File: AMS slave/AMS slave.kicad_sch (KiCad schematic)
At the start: 64 parts, among them J2 Conn_02x03_Odd_Even, J3 Conn_01x05, J4 Conn_01x05, Q2 AO3402, Q3 NCE60P04Y, SW2 SW_Push, U2 ATmega328P-A, U3 MCP2515-xST, U4 ISO1050DUB, U5 B0505MT-1WR4, U6 TPS54302, Y1 20MHz, Y2 8MHz

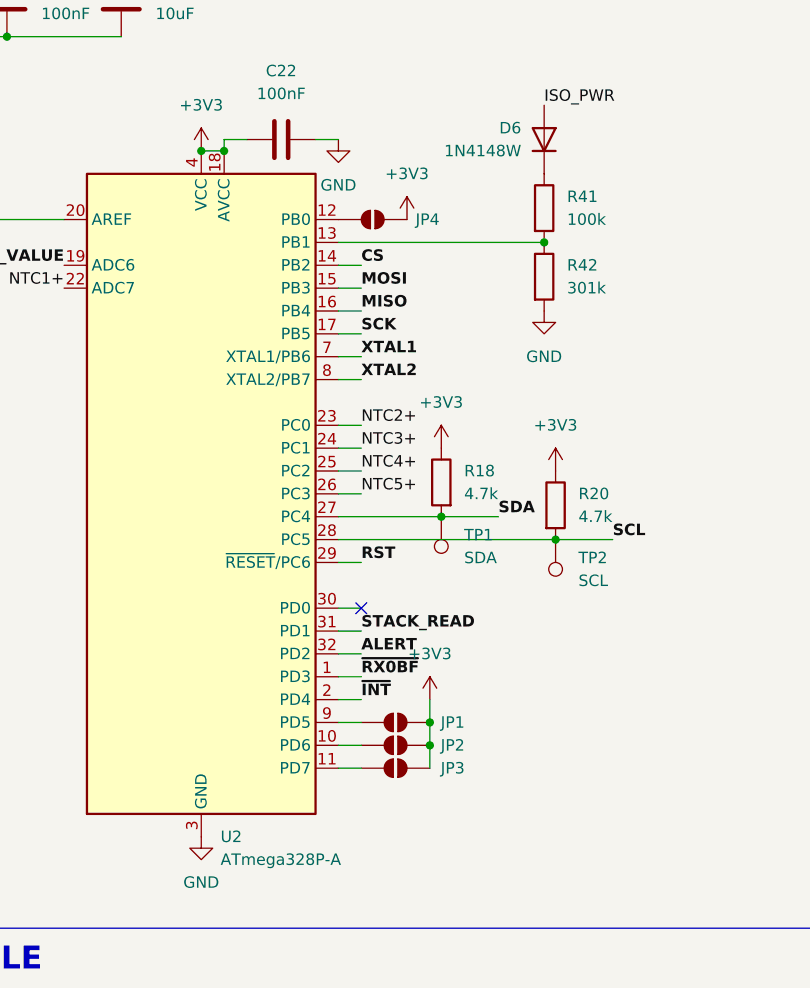
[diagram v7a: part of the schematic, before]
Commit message: Made slave select pads pull down
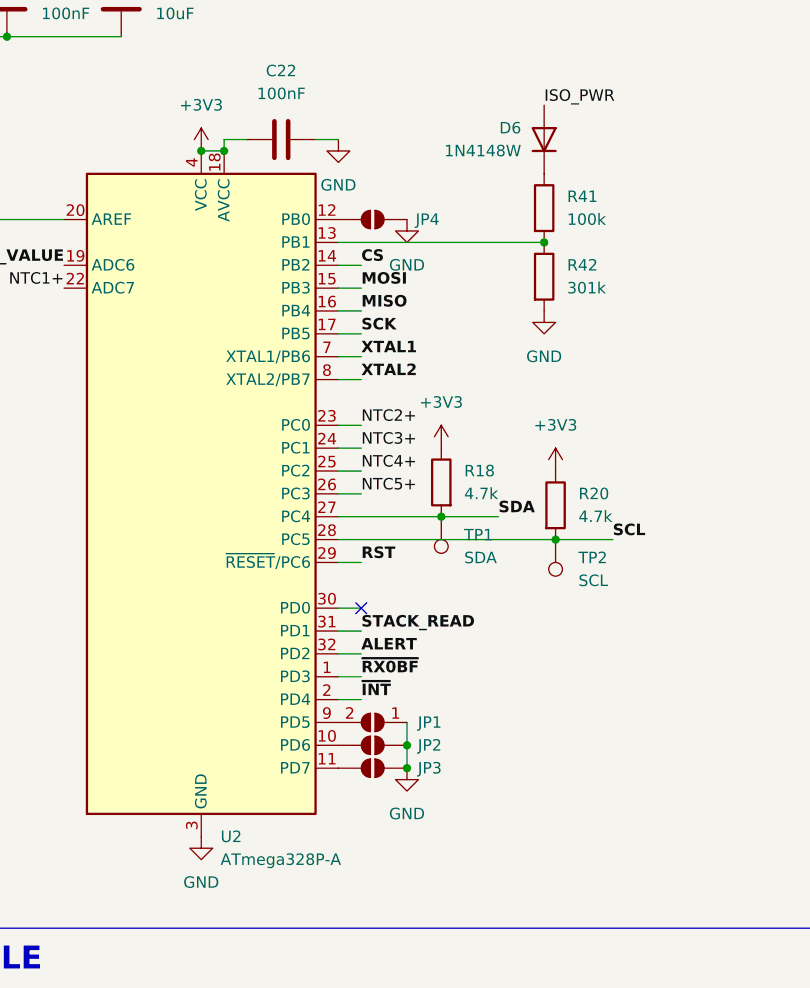
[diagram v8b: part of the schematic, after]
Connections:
- net +3V3: no longer JP1.2 (B), JP2.2 (B), JP3.2 (B), JP4.2 (B)
- net GND: now also JP1.1 (A), JP2.1 (A), JP3.1 (A), JP4.1 (A)
- net at U2.10 (PD6): now also JP2.2 (B); no longer JP2.1 (A)
- net at U2.11 (PD7): now also JP3.2 (B); no longer JP3.1 (A)
- net at U2.9 (PD5): now also JP1.2 (B); no longer JP1.1 (A)
- net at U2.12 (PB0): now also JP4.2 (B); no longer JP4.1 (A)
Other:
- moved on the sheet: JP2, JP3
